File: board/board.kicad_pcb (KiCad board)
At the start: 2 copper layers, 50 x 81 mm, 70 parts, among them IC1 tps610981dser, IC2 LTR-303ALS-01, IC3 EFM32TG108F32, J1 Conn_01x05_Male, J2 , J3 , J4 , Q1 Q_PMOS_GSD, SW2 SW_SPST

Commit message: connector routing nearly done
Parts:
- moved J1 16.3 mm to (111.9, 68.7)
- moved L2 2.95 mm to (111.8, 76.8)
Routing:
- net VREG: track 96.0 -> 128.0 mm
- net RESET: track 28.0 -> 51.2 mm
- net SWDIO: track 1.80 -> 13.9 mm
- net SWCLK: track 2.64 -> 7.67 mm
- net VBAT: track 62.6 -> 66.8 mm
- net REGMODE: track 84.0 -> 86.7 mm
- net Net-(L2-Pad2): track 4.05 -> 2.21 mm
- net GND: track 76.8 -> 77.9 mm, vias 35 -> 36

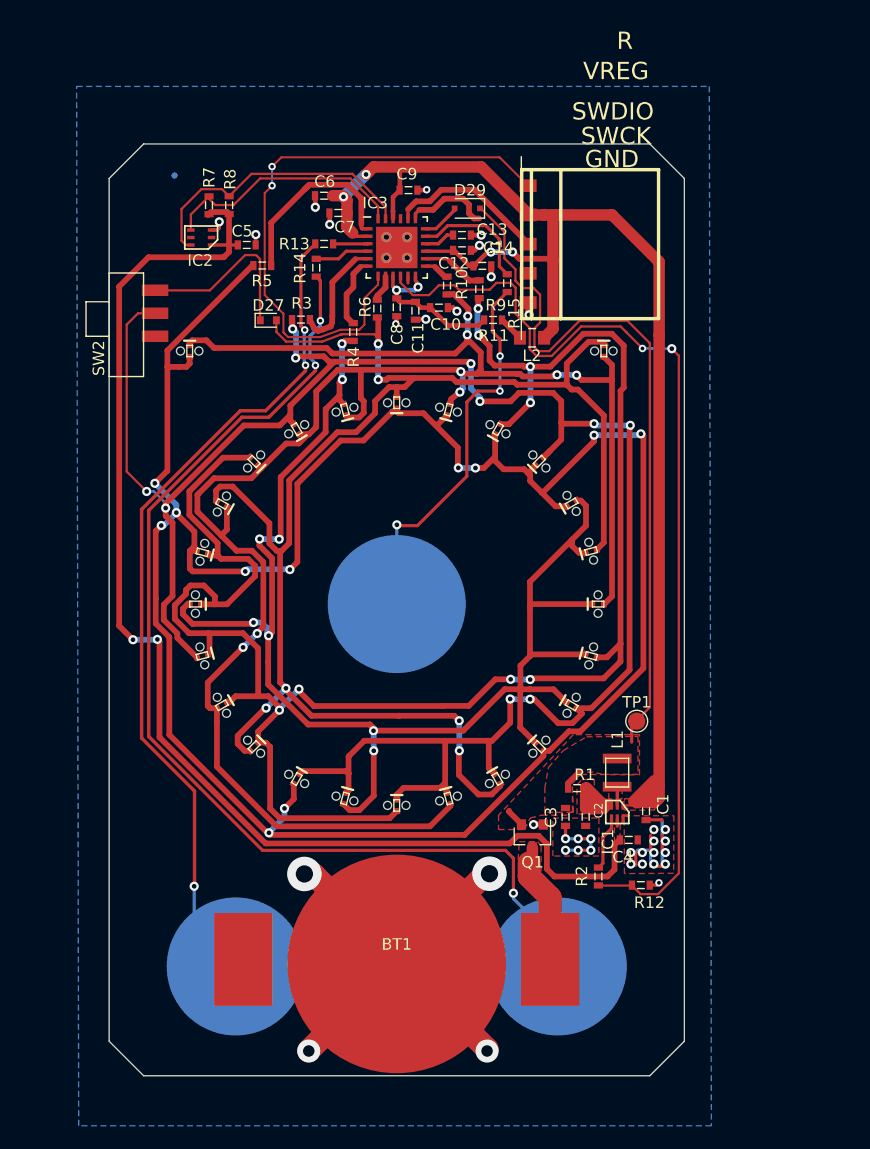
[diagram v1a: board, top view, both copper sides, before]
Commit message: figure out where to put temp sensor
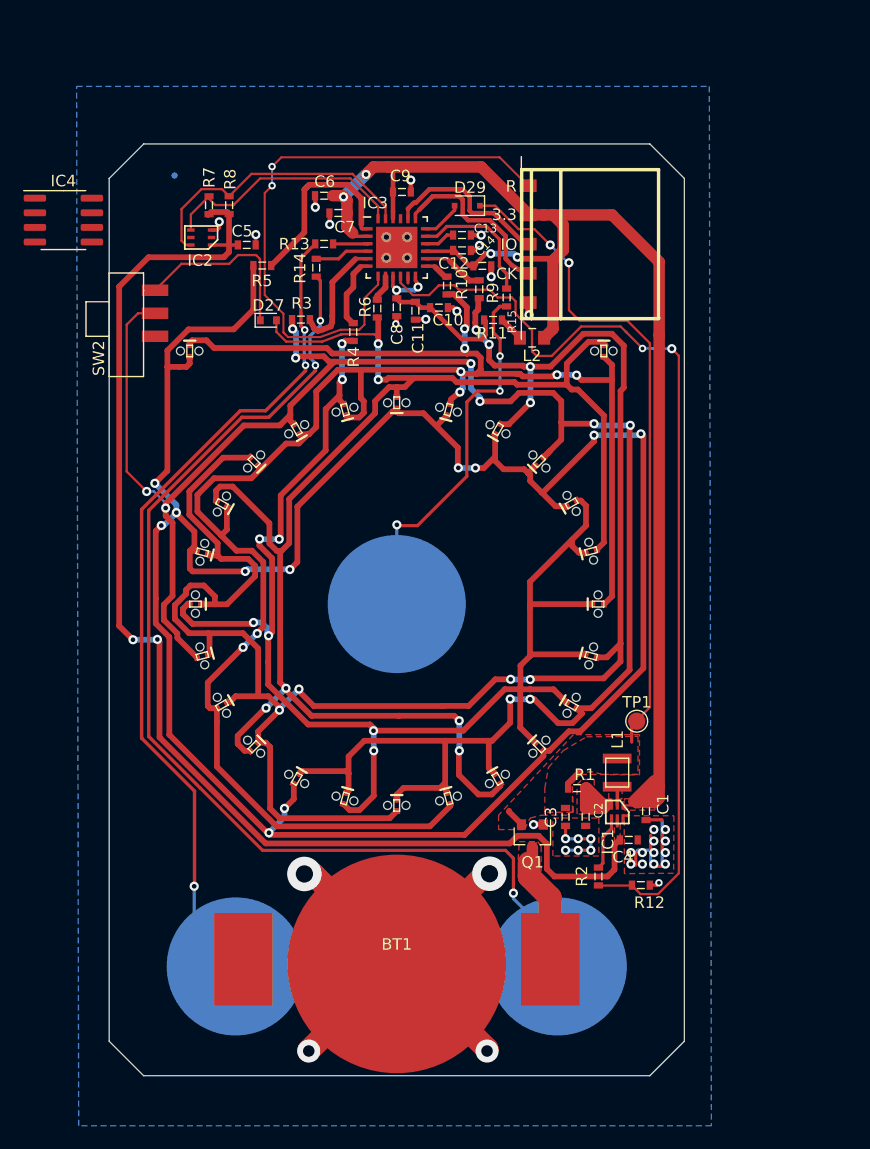
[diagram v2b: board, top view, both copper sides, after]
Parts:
- added IC4: AT30TS74-SS8M-B, Package_SO:SOIC-8_3.9x4.9mm_P1.27mm, F.Cu at (71.0, 66.6)
- moved R15 1.25 mm to (109.5, 73.3)
- moved C9 0.59 mm to (100.5, 64.2)
- moved D29 0.23 mm to (106.1, 65.4)
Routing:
- net SWCLK: track 7.67 -> 15.9 mm
- net VBAT: track 66.8 -> 61.8 mm, vias 0 -> 2
- net AVREG: track 14.3 -> 16.2 mm
- net REGMODE: track 86.7 -> 85.5 mm
- net Net-(IC3-Pad17): track 10.6 -> 11.8 mm
- net DPIN6: track 196.4 -> 197.4 mm
- net S3: track 33.9 -> 32.9 mm
- net DPIN2: track 165.8 -> 164.9 mm
- net DPIN1: track 135.3 -> 134.3 mm
- net VREG: track 128.0 -> 128.9 mm
- net SWDIO: track 13.9 -> 14.8 mm
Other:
- board text added: "3.3"
- board text added: "CK"
- board text added: "IO"
- board text removed: "GND"
- board text removed: "SWCK"
- board text removed: "SWDIO"
- board text removed: "VREG"

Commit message: routing done
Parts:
- moved IC4 15.0 mm to (84.4, 73.4), turned to 180 degrees
- moved D27 1.50 mm to (88.9, 76.8)
- moved R5 0.52 mm to (88.5, 70.1)
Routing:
- net SDA: track 25.4 -> 42.7 mm
- net SCL: track 21.8 -> 33.2 mm
- net GND: track 78.1 -> 85.7 mm, vias 36 -> 38
- net PVREG: track 111.3 -> 115.5 mm
- net DPIN6: track 197.4 -> 199.0 mm, vias 11 -> 13
- net DPIN1: track 134.3 -> 133.0 mm
- net Net-(IC3-Pad1): track 16.9 -> 16.0 mm

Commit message: tweaks
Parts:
- removed C12: 10u, mlm:0603
- added C12>: 10u, mlm:0603, F.Cu at (107.4, 70.6)
- renumbered R15 to R15>
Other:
- board text added: "+"
- board text added: "-"
- board text added: "EXP"
- board text added: "ISO"
- board text removed: "FIX EXP"
- board text removed: "FIX ISO"

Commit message: tweaks
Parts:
- renumbered R15> to R15
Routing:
- net GND: vias 38 -> 42
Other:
- board text added: "G"
- board text added: "V"
- board text removed: "3.3"

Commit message: tweaks
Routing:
- net GND: track 85.7 -> 105.7 mm, vias 42 -> 43
- net S3: track 33.1 -> 31.9 mm
- net S1: track 95.1 -> 96.3 mm
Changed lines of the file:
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@@
     (thickness 1.6)
     (drawings 76)
-    (tracks 1136)
+    (tracks 1153)
     (modules 71)
     (nets 43)
@@
   (page "A4")
   (layers
-    (0 "F.Cu" signal hide)
+    (0 "F.Cu" signal)
     (31 "B.Cu" signal)
     (32 "B.Adhes" user)
@@
   )
   (setup
-    (last_trace_width 0.3)
+    (last_trace_width 0.5)
     (user_trace_width 0.18)
     (user_trace_width 0.2)
@@
     (user_trace_width 2)
     (trace_clearance 0.2)
-    (zone_clearance 0.2)
-    (zone_45_only no)
+    (zone_clearance 0)
+    (zone_45_only yes)
     (trace_min 0.18)
     (via_size 0.8)
@@
       (other_layers_text_dims (size 1 1) (thickness 0.15) keep_upright)
     )
-    (pad_size 12 12)
+    (pad_size 1.8 1.8)
     (pad_drill 0)
     (pad_to_mask_clearance 0.0254)
@@
   (gr_line (start 123 62) (end 123 139) (layer "Dwgs.User") (width 0.1))
   (gr_line (start 77 62) (end 123 62) (layer "Dwgs.User") (width 0.1))
-  (gr_circle (center 100 100) (end 106 100) (layer "B.SilkS") (width 1))
+  (gr_circle (center 100 100) (end 107.24 100) (layer "B.SilkS") (width 2.6))
   (gr_text "20" (at 103.81 85.74 75) (layer "B.SilkS")
     (effects (font (size 1.75 1.75) (thickness 0.4375)) (justify mirror))
@@
     (effects (font (size 2 2) (thickness 0.15)) (justify mirror))
   )
-  (gr_circle (center 114 131.5) (end 120 131.5) (layer "B.SilkS") (width 1))
-  (gr_circle (center 86 131.5) (end 92 131.5) (layer "B.SilkS") (width 1))
+  (gr_circle (center 114 131.5) (end 121.24 131.5) (layer "B.SilkS") (width 2.5))
+  (gr_circle (center 86 131.5) (end 93.24 131.5) (layer "B.SilkS") (width 2.5))
   (gr_text "EXP" (at 77.97 76.92) (layer "B.SilkS")
     (effects (font (size 1 1) (thickness 0.15)) (justify mirror))
@@
   (gr_line (start 78 141) (end 122 141) (layer "Edge.Cuts") (width 0.05))
   (gr_circle (center 100 100) (end 117.5 100) (layer "B.SilkS") (width 0.5))
+  (via (at 110.14 127.5) (size 0.8) (drill 0.4) (layers "F.Cu" "B.Cu") (net 16))
+  (segment (start 110.14 127.5) (end 112.04 127.5) (width 0.28) (layer "B.Cu") (net 16))
+  (segment (start 112.04 127.5) (end 114 129.46) (width 0.28) (layer "B.Cu") (net 16))
+  (segment (start 114 129.46) (end 114 131.5) (width 0.28) (layer "B.Cu") (net 16))
+  (segment (start 110.14 127.5) (end 110.14 122.1) (width 0.28) (layer "F.Cu") (net 16))
+  (segment (start 110.14 122.1) (end 109.45 121.41) (width 0.28) (layer "F.Cu") (net 16))
+  (segment (start 109.45 121.41) (end 88.34 121.41) (width 0.28) (layer "F.Cu") (net 16))
+  (segment (start 88.34 121.41) (end 82.92 115.99) (width 0.28) (layer "F.Cu") (net 16))
+  (segment (start 82.92 115.99) (end 82.64 115.71) (width 0.28) (layer "F.Cu") (net 16))
+  (segment (start 82.45 127.25) (end 82.39 127.31) (width 0.28) (layer "B.Cu") (net 15))
+  (segment (start 82.42 124.53) (end 82.42 127.22) (width 0.3) (layer "F.Cu") (net 15))
+  (via (at 82.45 127.25) (size 0.8) (drill 0.4) (layers "F.Cu" "B.Cu") (net 15))
+  (segment (start 82.39 127.31) (end 82.39 127.89) (width 0.28) (layer "B.Cu") (net 15))
+  (segment (start 82.39 127.89) (end 86 131.5) (width 0.28) (layer "B.Cu") (net 15))
+  (segment (start 82.42 127.22) (end 82.45 127.25) (width 0.28) (layer "F.Cu") (net 15))
+  (segment (start 100 94.45) (end 106.09 88.36) (width 0.28) (layer "F.Cu") (net 37))
+  (segment (start 106.09 88.36) (end 106.09 82.44) (width 0.28) (layer "F.Cu") (net 37))
+  (segment (start 106.09 82.44) (end 107.05 81.48) (width 0.28) (layer "F.Cu") (net 37))
+  (segment (start 107.05 81.48) (end 108.97 81.48) (width 0.28) (layer "F.Cu") (net 37))
+  (via (at 100 94.45) (size 0.8) (drill 0.4) (layers "F.Cu" "B.Cu") (net 37))
+  (segment (start 100 94.45) (end 100 100) (width 0.28) (layer "B.Cu") (net 37))
+  (via (at 99.95 69.05) (size 0.8) (drill 0.4) (layers "F.Cu" "B.Cu") (net 9))
+  (segment (start 99.95 69.05) (end 99.95 68.95) (width 0.5) (layer "B.Cu") (net 9))
+  (segment (start 99.95 69.85) (end 99.95 69.05) (width 0.5) (layer "B.Cu") (net 9))
+  (segment (start 97.5 69.05) (end 99.85 69.05) (width 0.5) (layer "B.Cu") (net 9))
+  (segment (start 99.85 69.05) (end 99.95 68.95) (width 0.5) (layer "B.Cu") (net 9))
+  (segment (start 99.1 69.85) (end 99.975 68.975) (width 0.5) (layer "B.Cu") (net 9))
+  (segment (start 99.975 68.975) (end 100.85 68.1) (width 0.5) (layer "B.Cu") (net 9))
+  (segment (start 102.15 69.05) (end 100.05 69.05) (width 0.5) (layer "B.Cu") (net 9))
+  (segment (start 100.05 69.05) (end 99.975 68.975) (width 0.5) (layer "B.Cu") (net 9))
+  (segment (start 99.1 68.1) (end 99.95 68.95) (width 0.5) (layer "B.Cu") (net 9))
+  (segment (start 99.95 68.95) (end 100.85 69.85) (width 0.5) (layer "B.Cu") (net 9))
+  (segment (start 99.95 68.1) (end 99.95 68.95) (width 0.5) (layer "B.Cu") (net 9))
+  (segment (start 99.95 69.85) (end 99.95 71.15) (width 0.5) (layer "B.Cu") (net 9))
+  (segment (start 99.95 68.1) (end 99.95 66.85) (width 0.5) (layer "B.Cu") (net 9))
+  (segment (start 100.85 69.85) (end 101.85 70.85) (width 0.5) (layer "B.Cu") (net 9))
+  (segment (start 99.1 69.85) (end 98.15 70.85) (width 0.5) (layer "B.Cu") (net 9))
+  (segment (start 99.1 68.1) (end 98.15 67.15) (width 0.5) (layer "B.Cu") (net 9))
+  (segment (start 100.85 68.1) (end 102.26 66.72) (width 0.5) (layer "B.Cu") (net 9))
   (via (at 99.1 69.85) (size 0.8) (drill 0.4) (layers "F.Cu" "B.Cu") (net 9))
   (via (at 100.85 69.85) (size 0.8) (drill 0.4) (layers "F.Cu" "B.Cu") (net 9))
@@
   (segment (start 105.36 88.17) (end 105.35 88.16) (width 0.5) (layer "B.Cu") (net 2))
   (via (at 105.35 88.16) (size 0.8) (drill 0.4) (layers "F.Cu" "B.Cu") (net 2))
-  (segment (start 108.97 81.48) (end 107.05 81.48) (width 0.28) (layer "F.Cu") (net 37))
-  (segment (start 106.09 82.44) (end 106.09 88.89) (width 0.28) (layer "F.Cu") (net 37))
-  (segment (start 106.09 88.89) (end 101.8 93.18) (width 0.28) (layer "F.Cu") (net 37))
-  (segment (start 107.05 81.48) (end 106.09 82.44) (width 0.28) (layer "F.Cu") (net 37))
-  (segment (start 101.8 93.18) (end 100.08 93.18) (width 0.28) (layer "F.Cu") (net 37))
-  (segment (start 100.08 93.18) (end 100.01 93.11) (width 0.28) (layer "F.Cu") (net 37))
   (via (at 101.85 72.44) (size 0.8) (drill 0.4) (layers "F.Cu" "B.Cu") (net 17))
   (segment (start 101.85 72.44) (end 101.75 72.34) (width 0.3) (layer "F.Cu") (net 17))
@@
   (segment (start 101.625 71.905) (end 101.625 71.5) (width 0.3) (layer "F.Cu") (net 17))
   (segment (start 101.58 72.71) (end 99.98 72.71) (width 0.4) (layer "B.Cu") (net 17))
-  (via (at 110.14 125.13) (size 0.8) (drill 0.4) (layers "F.Cu" "B.Cu") (net 16))
-  (segment (start 114 129.46) (end 114 131.5) (width 0.28) (layer "B.Cu") (net 16))
-  (segment (start 82.92 115.99) (end 82.64 115.71) (width 0.28) (layer "F.Cu") (net 16))
-  (segment (start 110.14 125.13) (end 110.14 125.6) (width 0.28) (layer "B.Cu") (net 16))
-  (segment (start 110.14 125.6) (end 114 129.46) (width 0.28) (layer "B.Cu") (net 16))
-  (segment (start 110.14 125.13) (end 110.14 122.1) (width 0.28) (layer "F.Cu") (net 16))
-  (segment (start 110.14 122.1) (end 109.45 121.41) (width 0.28) (layer "F.Cu") (net 16))
-  (segment (start 88.34 121.41) (end 82.92 115.99) (width 0.28) (layer "F.Cu") (net 16))
-  (segment (start 109.45 121.41) (end 88.34 121.41) (width 0.28) (layer "F.Cu") (net 16))
   (segment (start 104.37059 116.417037) (end 104.18 115.56) (width 0.5) (layer "F.Cu") (net 5))
   (segment (start 104.74 82.17) (end 104.62941 82.617037) (width 0.5) (layer "F.Cu") (net 3))
@@
   (segment (start 99.27 80.34) (end 99.12 80.49) (width 0.5) (layer "F.Cu") (net 1))
   (segment (start 99.12 80.49) (end 98.39 80.49) (width 0.5) (layer "F.Cu") (net 1))
-  (segment (start 82.39 124.53) (end 82.39 127.89) (width 0.28) (layer "B.Cu") (net 15))
-  (segment (start 82.39 127.89) (end 86 131.5) (width 0.28) (layer "B.Cu") (net 15))
-  (segment (start 82.42 124.53) (end 82.39 124.53) (width 0.28) (layer "F.Cu") (net 15))
-  (via (at 82.39 124.53) (size 0.8) (drill 0.4) (layers "F.Cu" "B.Cu") (net 15))
   (via (at 95.24 77.37) (size 0.8) (drill 0.4) (layers "F.Cu" "B.Cu") (net 6))
   (segment (start 95.24 77.37) (end 95.51 77.1) (width 0.5) (layer "F.Cu") (net 6))
@@
   (segment (start 81.665 68.785) (end 81.29 68.41) (width 0.2) (layer "F.Cu") (net 8))
   (segment (start 109.77 117.96) (end 109.77 118.06) (width 0.5) (layer "F.Cu") (net 11))
-  (via (at 100.01 93.11) (size 0.8) (drill 0.4) (layers "F.Cu" "B.Cu") (net 37))
-  (segment (start 100 93.12) (end 100.01 93.11) (width 0.28) (layer "B.Cu") (net 37))
-  (segment (start 100 100) (end 100 93.12) (width 0.28) (layer "B.Cu") (net 37))
   (segment (start 105.41 79.63) (end 96.88 79.63) (width 0.5) (layer "F.Cu") (net 3))
   (segment (start 105.57 79.79) (end 105.41 79.63) (width 0.5) (layer "F.Cu") (net 3))
@@
       )
     )
+  )
+  (zone (net 0) (net_name "") (layer "B.Cu") (hatch edge 0.508)
+    (connect_pads yes (clearance 0))
+    (min_thickness 0.254)
+    (keepout (tracks allowed) (vias allowed) (copperpour not_allowed))
+    (fill (mode hatch) (thermal_gap 0.508) (thermal_bridge_width 0.508)
+      (hatch_thickness 0.5) (hatch_gap 0.5) (hatch_orientation 0))
+    (polygon
+      (pts
+        (xy 98.15 67.15) (xy 101.85 67.15) (xy 101.85 70.85) (xy 98.15 70.85)
+      )
+    )

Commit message: minor
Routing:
- net VREG: track 128.9 -> 125.9 mm
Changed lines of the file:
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@@
   (gr_line (start 78 141) (end 122 141) (layer "Edge.Cuts") (width 0.05))
   (gr_circle (center 100 100) (end 117.5 100) (layer "B.SilkS") (width 0.5))
+  (segment (start 113.58 66.17) (end 113.62 66.17) (width 1) (layer "F.Cu") (net 10))
+  (segment (start 113.62 66.17) (end 122.81 75.36) (width 1) (layer "F.Cu") (net 10))
+  (segment (start 122.81 75.36) (end 122.81 76.61) (width 1) (layer "F.Cu") (net 10))
+  (segment (start 122.81 76.61) (end 122.81 115.8) (width 1) (layer "F.Cu") (net 10))
   (via (at 110.14 127.5) (size 0.8) (drill 0.4) (layers "F.Cu" "B.Cu") (net 16))
   (segment (start 110.14 127.5) (end 112.04 127.5) (width 0.28) (layer "B.Cu") (net 16))
@@
   (segment (start 120.86 110.11) (end 122 108.97) (width 0.2) (layer "F.Cu") (net 11))
   (segment (start 113.58 70.13) (end 113.58 76.08) (width 1) (layer "F.Cu") (net 10))
-  (segment (start 113.58 66.17) (end 118.72 66.17) (width 1) (layer "F.Cu") (net 10))
   (segment (start 112.77 66.17) (end 113.58 66.17) (width 1) (layer "F.Cu") (net 10))
   (segment (start 113.58 76.08) (end 112.81 76.85) (width 1) (layer "F.Cu") (net 10))
   (segment (start 112.81 76.85) (end 112.9 76.85) (width 1) (layer "F.Cu") (net 10))
   (segment (start 111.41 66.17) (end 112.77 66.17) (width 1) (layer "F.Cu") (net 10))
-  (segment (start 118.72 66.17) (end 122.81 70.26) (width 1) (layer "F.Cu") (net 10))
-  (segment (start 122.81 70.26) (end 122.81 76.61) (width 1) (layer "F.Cu") (net 10))
   (segment (start 112.81 76.85) (end 113.03 76.63) (width 0.5) (layer "F.Cu") (net 10))
   (segment (start 109.145 75.3) (end 109.16 75.3) (width 0.5) (layer "F.Cu") (net 18))
@@
   (segment (start 122.31 116.3) (end 122.81 115.8) (width 0.5) (layer "F.Cu") (net 10))
   (segment (start 122.28 116.3) (end 122.31 116.3) (width 0.5) (layer "F.Cu") (net 10))
-  (segment (start 122.81 115.8) (end 122.81 76.61) (width 1) (layer "F.Cu") (net 10))
   (segment (start 122.81 116.86) (end 122.81 115.8) (width 1) (layer "F.Cu") (net 10))
   (segment (start 120.77 117.5) (end 120.77 117.23) (width 0.5) (layer "F.Cu") (net 10))

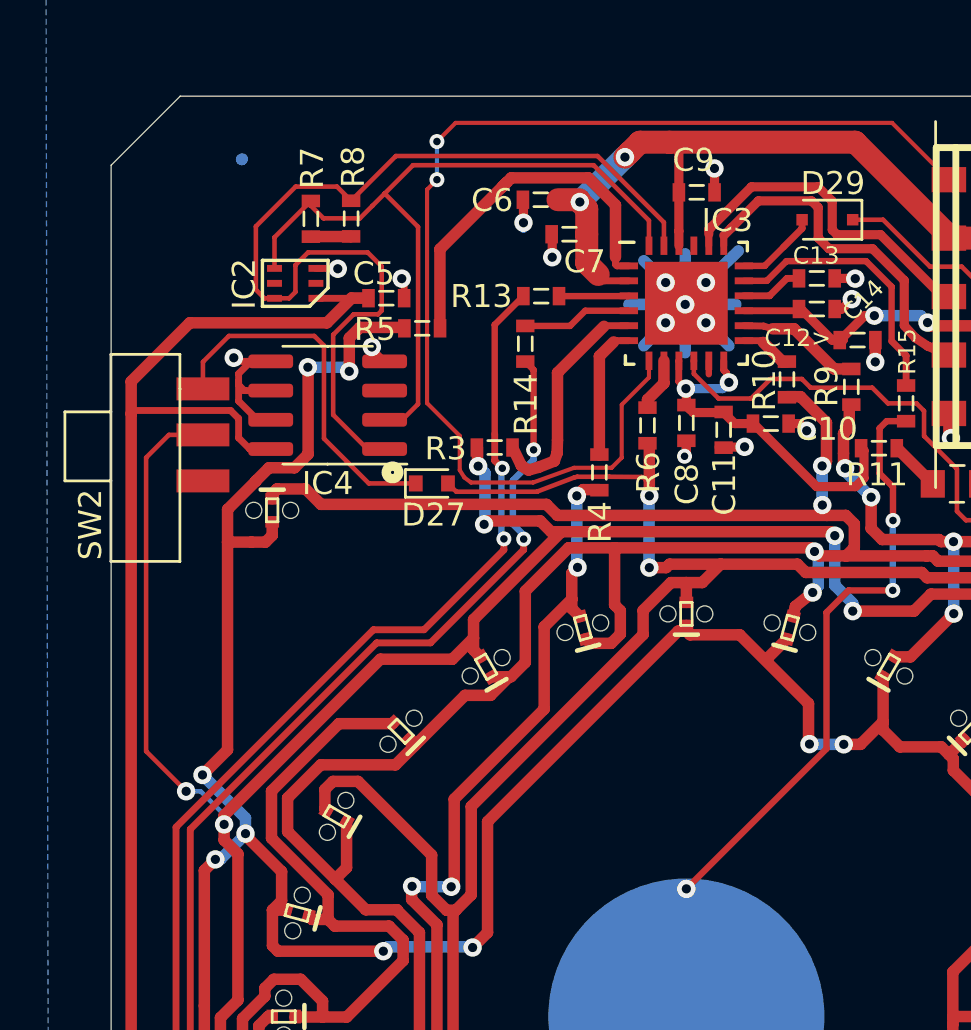
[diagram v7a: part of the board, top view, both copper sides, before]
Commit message: fix light sensor routing
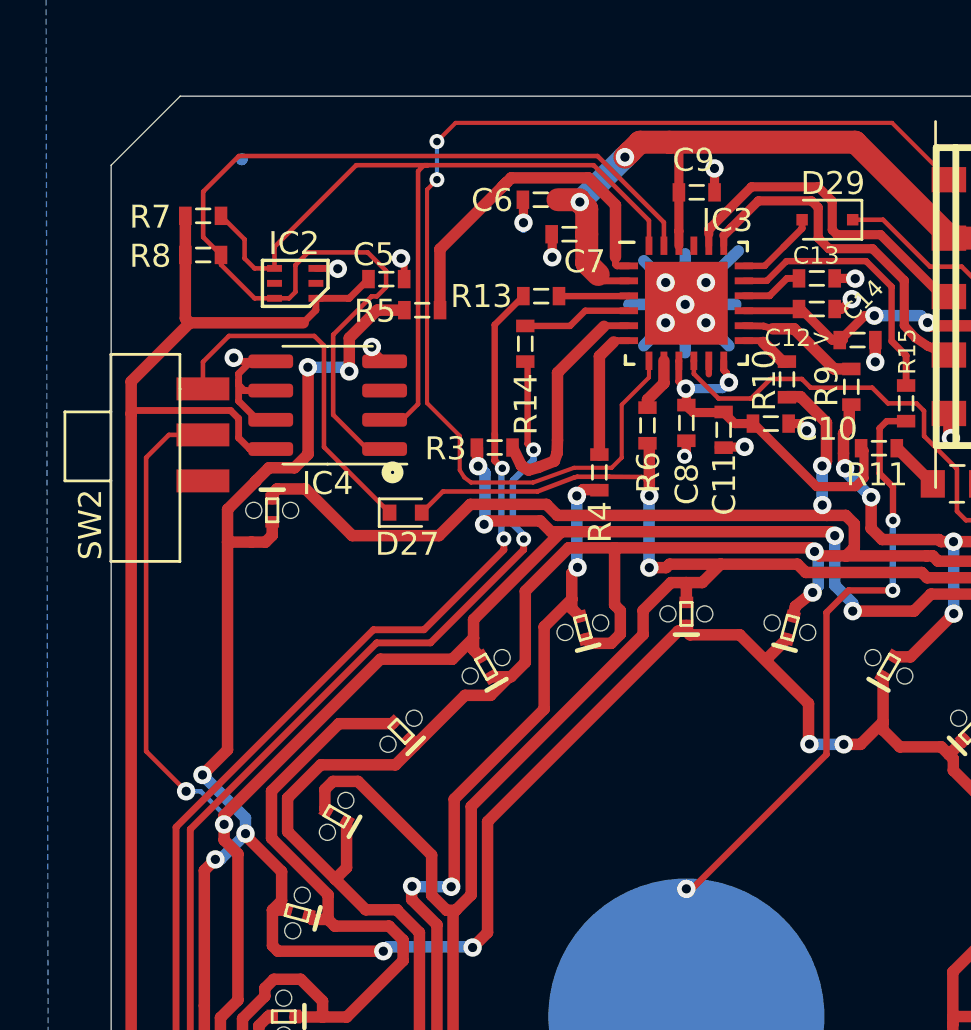
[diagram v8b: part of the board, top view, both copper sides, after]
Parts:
- moved R8 6.62 mm to (79.0, 66.9), turned to 0 degrees
- moved R7 4.68 mm to (79.0, 65.2), turned to 0 degrees
- moved D27 1.71 mm to (87.8, 78.1)
- moved C5 0.83 mm to (87.0, 68.0)
- moved R5 0.79 mm to (88.5, 69.3)
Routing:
- net SCL: track 33.2 -> 36.9 mm
- net SDA: track 42.7 -> 46.2 mm
- net DPIN1: track 133.0 -> 134.4 mm
- net PVREG: track 115.5 -> 116.7 mm
- net DPIN2: track 164.9 -> 166.0 mm
- net Net-(IC3-Pad1): track 16.0 -> 15.5 mm
